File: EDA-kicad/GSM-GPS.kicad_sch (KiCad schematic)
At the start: 2 parts, among them J3 SIM-G85D1160022HHR, U9 GSM-GPS-EC25VFA-512-STD

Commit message: add caution message
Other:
- note added: "Take care when choosing variants for different continents"
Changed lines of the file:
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@@
+		)
+	)
+	(text "Take care when choosing variants for different continents"
+		(exclude_from_sim no)
+		(at 163.576 26.67 0)
+		(effects
+			(font
+				(size 1.27 1.27)
+			)
 		)
 	)

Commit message: add EG25 new gpsgsm
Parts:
- added U1: EG25GGC-128-SGNS, SPIRIT-footprints:XCVR_EG25GGC-128-SGNS, symbol SPIRIT-components:EG25GGC-128-SGNS
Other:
- moved on the sheet: U9

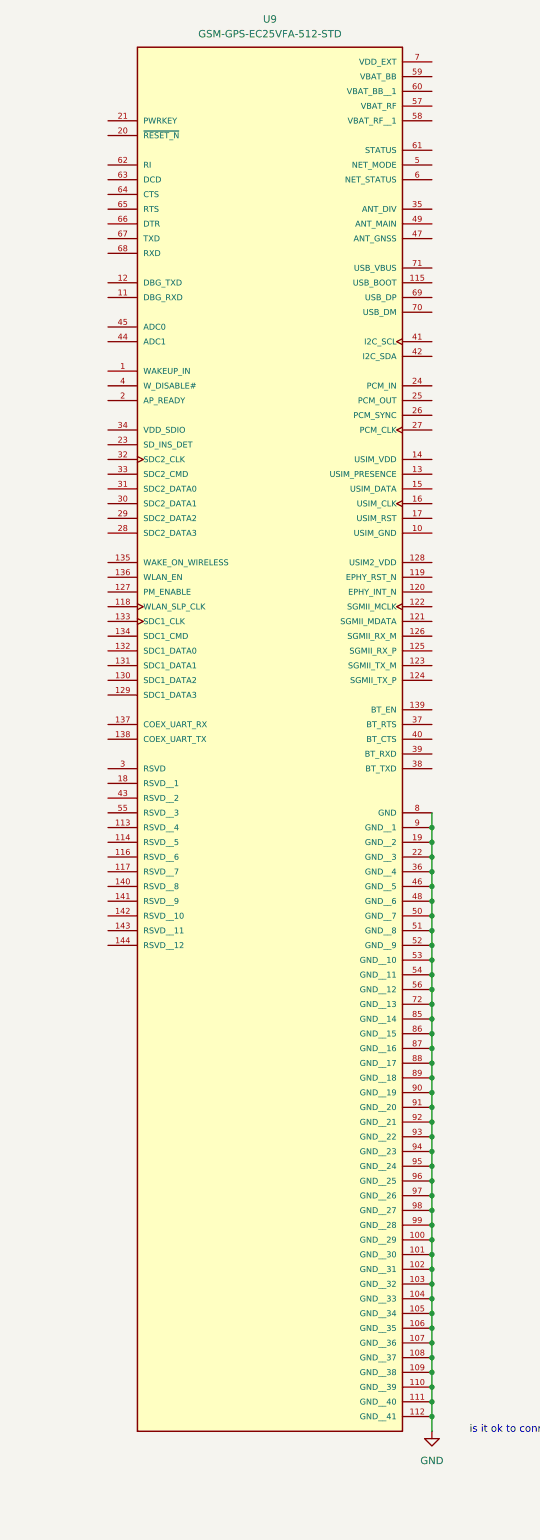
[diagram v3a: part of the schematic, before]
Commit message: exclude old EC25 and minor changes to power
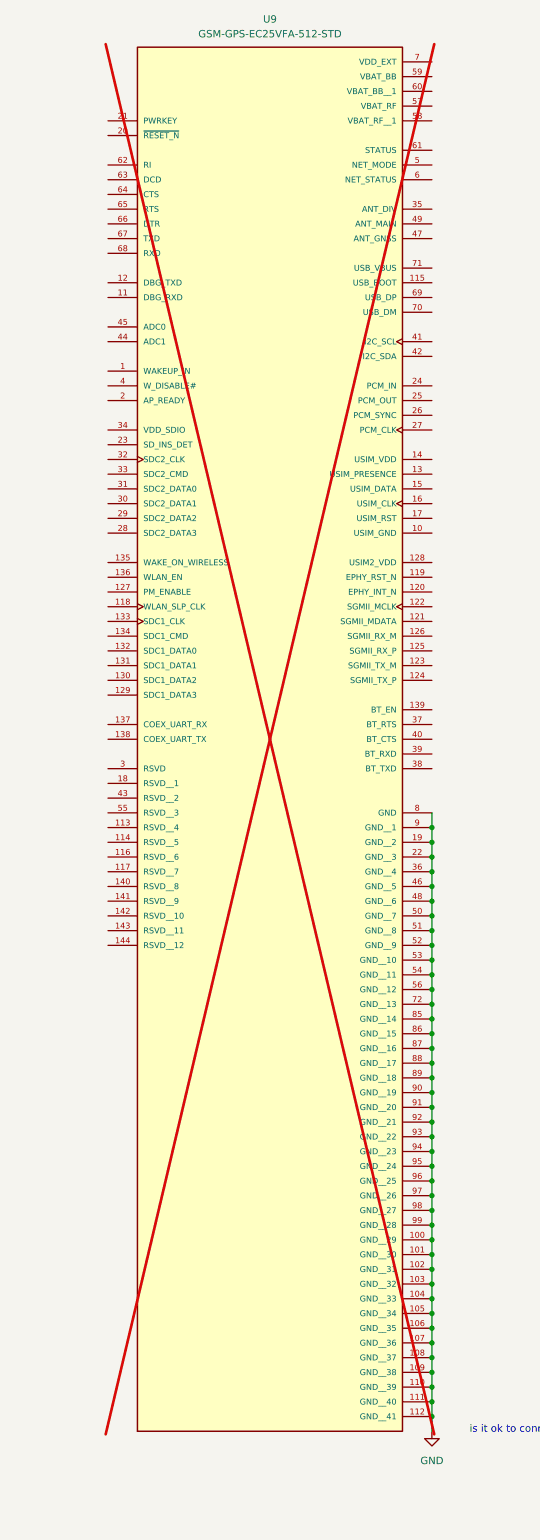
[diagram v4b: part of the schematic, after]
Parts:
- U9: now not fitted; now left out of the parts list
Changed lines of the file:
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@@
 		(unit 1)
 		(exclude_from_sim no)
-		(in_bom yes)
-		(on_board yes)
-		(dnp no)
+		(in_bom no)
+		(on_board no)
+		(dnp yes)
 		(fields_autoplaced yes)
 		(property "Reference" "U9"

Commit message: add note (test commit)
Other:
- note added: "need to be careful if 128 and 256 symbols and footprints are identical TODO rename them and double check"
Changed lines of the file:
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@@
+		)
+	)
+	(text "need to be careful if 128 and 256 symbols and footprints are identical\n\nTODO rename them and double check"
+		(exclude_from_sim no)
+		(at 168.402 84.582 0)
+		(effects
+			(font
+				(size 1.27 1.27)
+			)
 		)
 	)

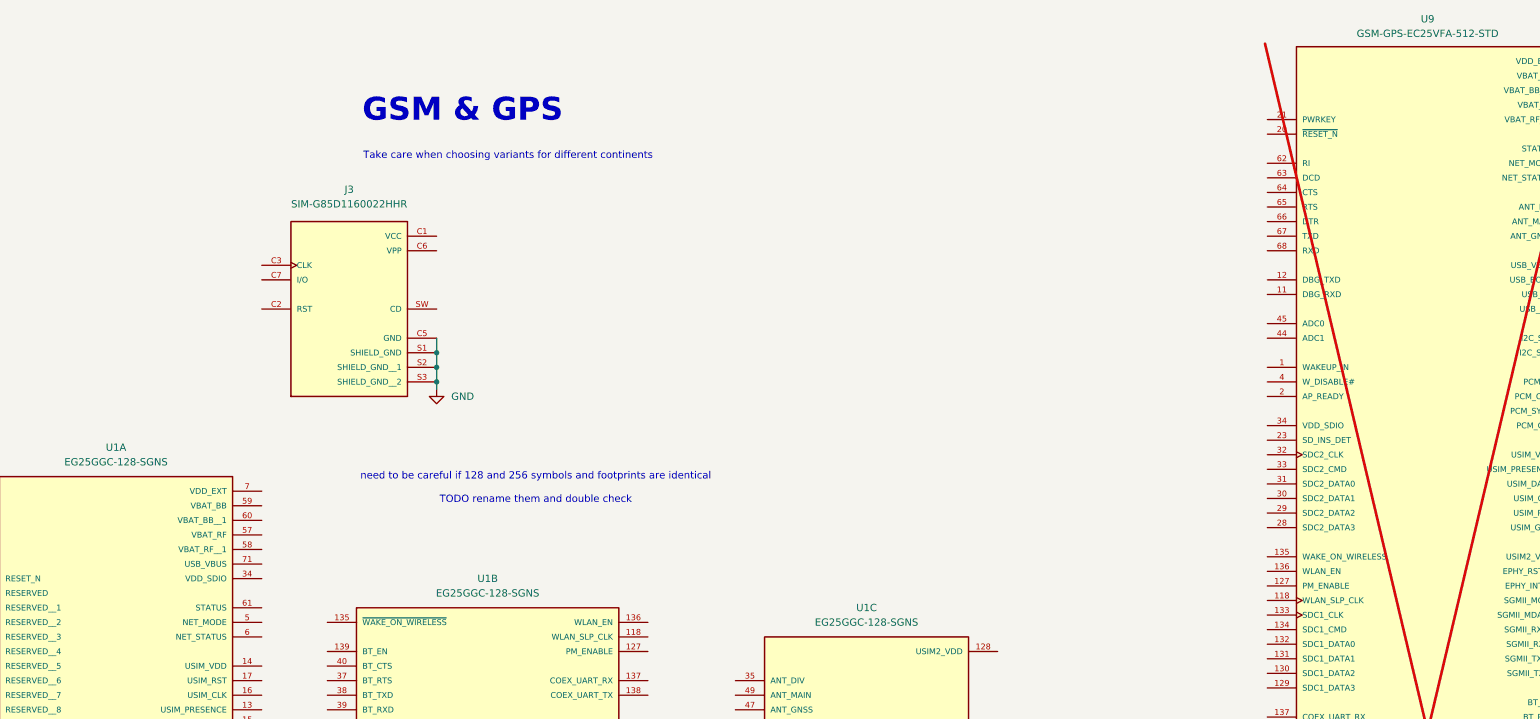
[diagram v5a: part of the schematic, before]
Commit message: reannotate entire schematic
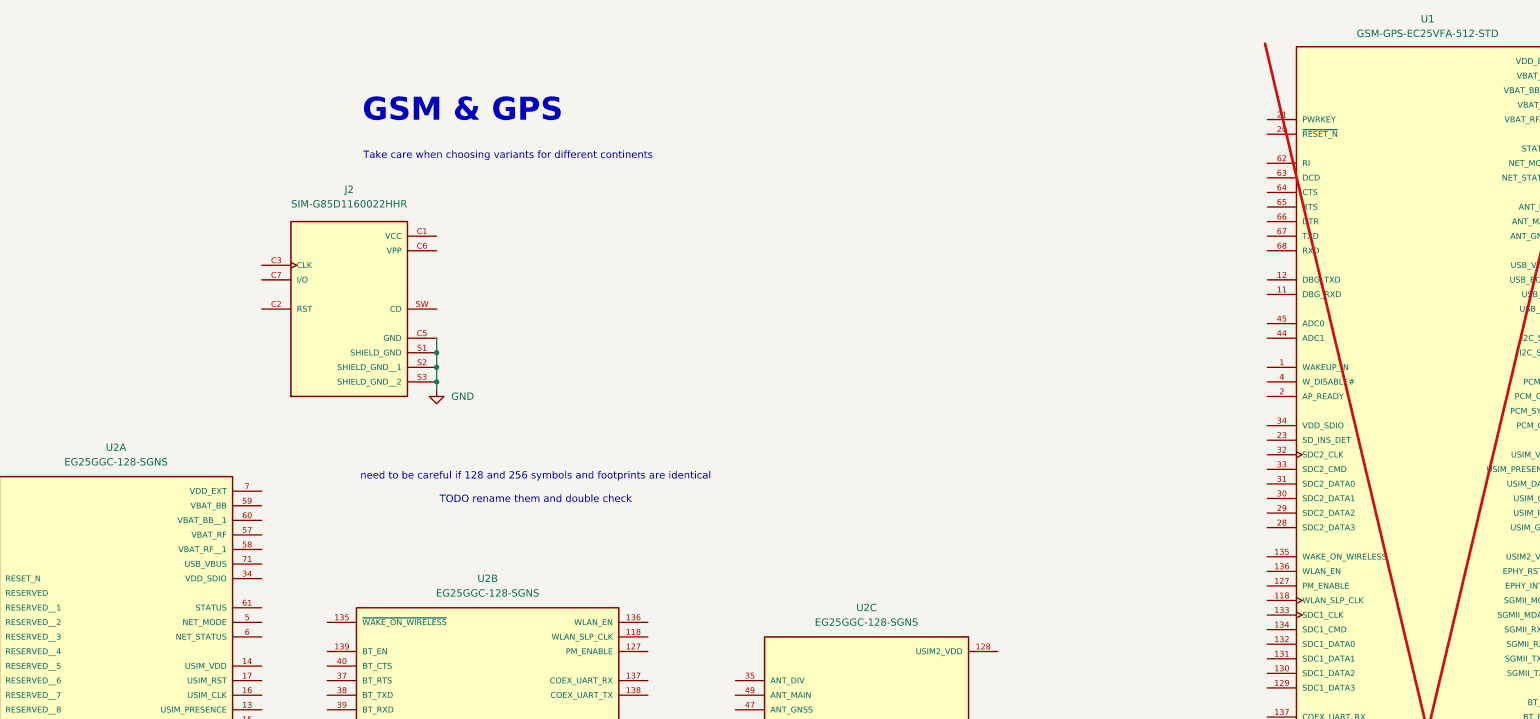
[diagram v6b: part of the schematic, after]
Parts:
- renumbered J3 to J2, U9 to U1, U1 to U2
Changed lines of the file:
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@@
 		(dnp no)
 		(fields_autoplaced yes)
-		(property "Reference" "J3"
+		(property "Reference" "J2"
 			(at 135.89 32.512 0)
 			(effects
@@
 			(project "cm5-carrier"
 				(path "/28c5e4fe-1ec7-4477-97f0-d2ec1401fad5/1297454b-0b1d-459e-9de1-2b16d7982efe"
-					(reference "J3")
+					(reference "J2")
 					(unit 1)
 				)
@@
 		(dnp no)
 		(fields_autoplaced yes)
-		(property "Reference" "U1"
+		(property "Reference" "U2"
 			(at 226.06 105.41 0)
 			(effects
@@
 			(project ""
 				(path "/28c5e4fe-1ec7-4477-97f0-d2ec1401fad5/1297454b-0b1d-459e-9de1-2b16d7982efe"
-					(reference "U1")
+					(reference "U2")
 					(unit 3)
 				)
@@
 		(dnp no)
 		(fields_autoplaced yes)
-		(property "Reference" "#PWR062"
+		(property "Reference" "#PWR063"
 			(at 151.13 73.66 0)
 			(effects
@@
 			(project "cm5-carrier"
 				(path "/28c5e4fe-1ec7-4477-97f0-d2ec1401fad5/1297454b-0b1d-459e-9de1-2b16d7982efe"
-					(reference "#PWR062")
+					(reference "#PWR063")
 					(unit 1)
 				)
@@
 		(dnp no)
 		(fields_autoplaced yes)
-		(property "Reference" "U1"
+		(property "Reference" "U2"
 			(at 95.25 77.47 0)
 			(effects
@@
 			(project ""
 				(path "/28c5e4fe-1ec7-4477-97f0-d2ec1401fad5/1297454b-0b1d-459e-9de1-2b16d7982efe"
-					(reference "U1")
+					(reference "U2")
 					(unit 1)
 				)
@@
 		(dnp yes)
 		(fields_autoplaced yes)
-		(property "Reference" "U9"
+		(property "Reference" "U1"
 			(at 323.85 2.794 0)
 			(effects
@@
 			(project "cm5-carrier"
 				(path "/28c5e4fe-1ec7-4477-97f0-d2ec1401fad5/1297454b-0b1d-459e-9de1-2b16d7982efe"
-					(reference "U9")
+					(reference "U1")
 					(unit 1)
 				)
@@
 		(dnp no)
 		(fields_autoplaced yes)
-		(property "Reference" "U1"
+		(property "Reference" "U2"
 			(at 160.02 100.33 0)
 			(effects
@@
 			(project ""
 				(path "/28c5e4fe-1ec7-4477-97f0-d2ec1401fad5/1297454b-0b1d-459e-9de1-2b16d7982efe"
-					(reference "U1")
+					(reference "U2")
 					(unit 2)
 				)
@@
 		(dnp no)
 		(fields_autoplaced yes)
-		(property "Reference" "#PWR066"
+		(property "Reference" "#PWR064"
 			(at 351.79 252.73 0)
 			(effects
@@
 			(project "cm5-carrier"
 				(path "/28c5e4fe-1ec7-4477-97f0-d2ec1401fad5/1297454b-0b1d-459e-9de1-2b16d7982efe"
-					(reference "#PWR066")
+					(reference "#PWR064")
 					(unit 1)
 				)

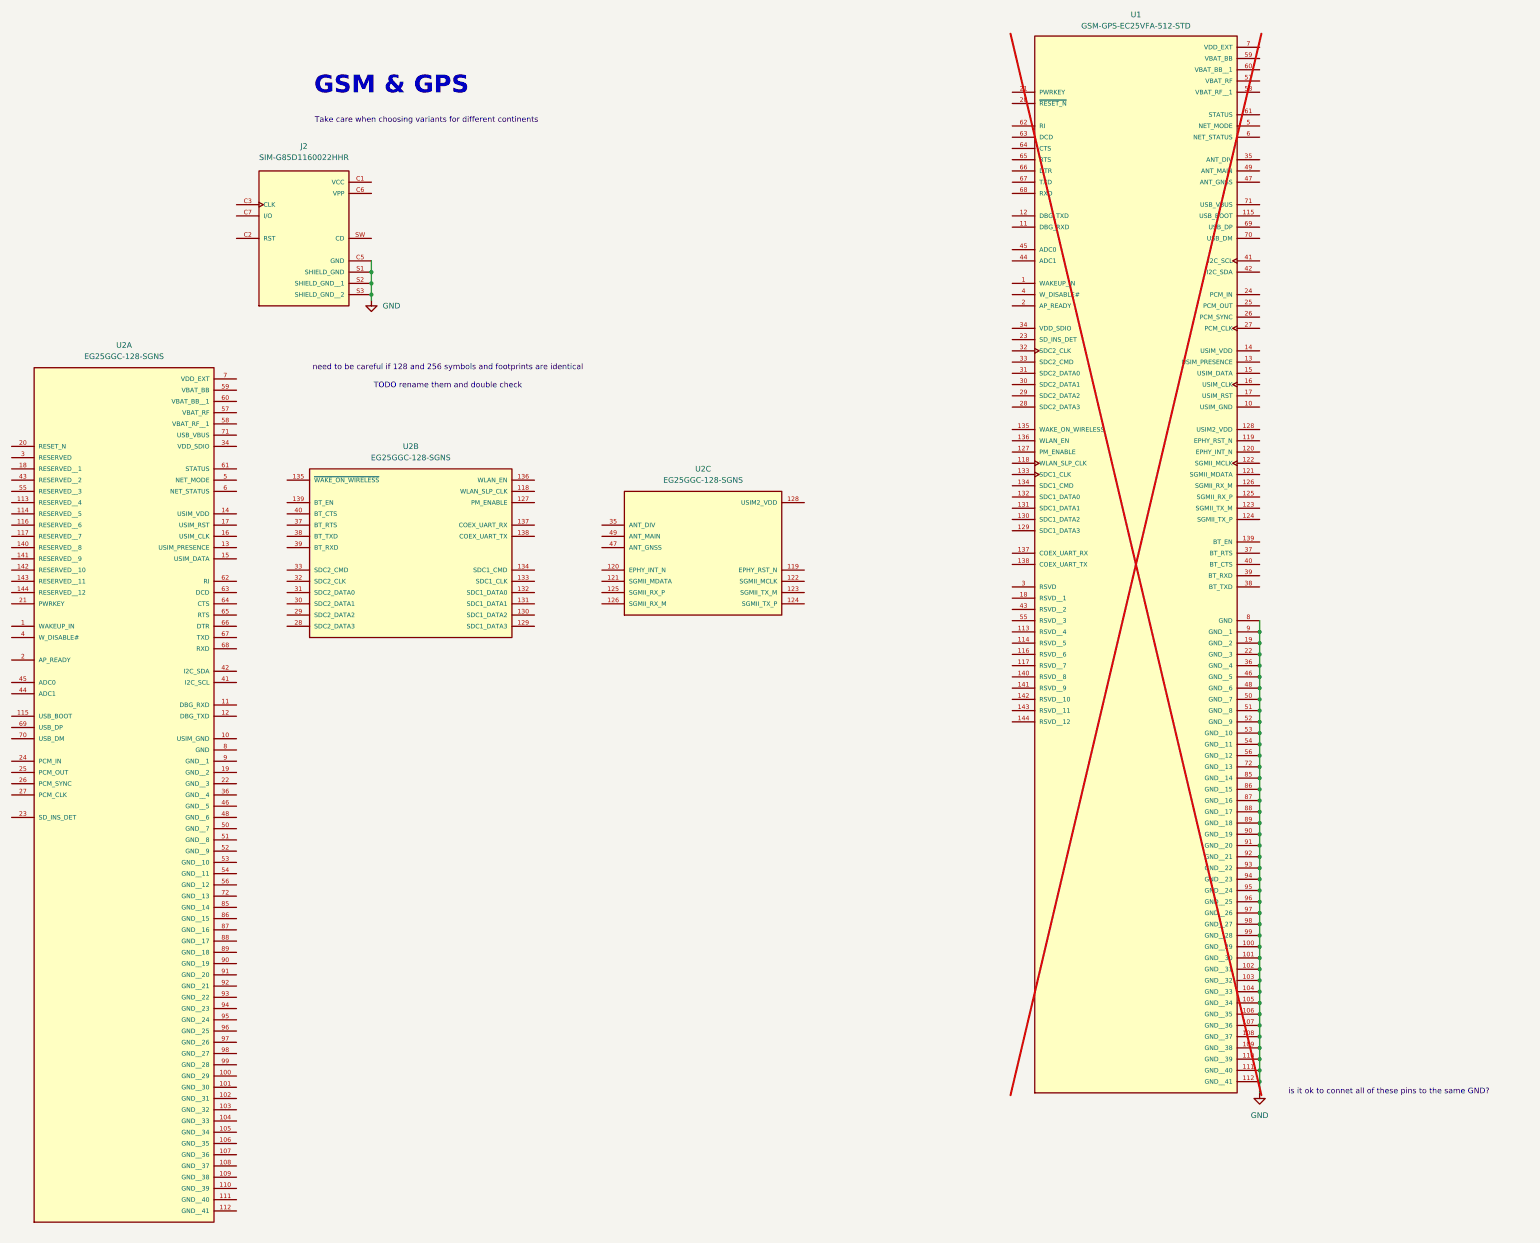
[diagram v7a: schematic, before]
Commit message: set everything except from power to DNP
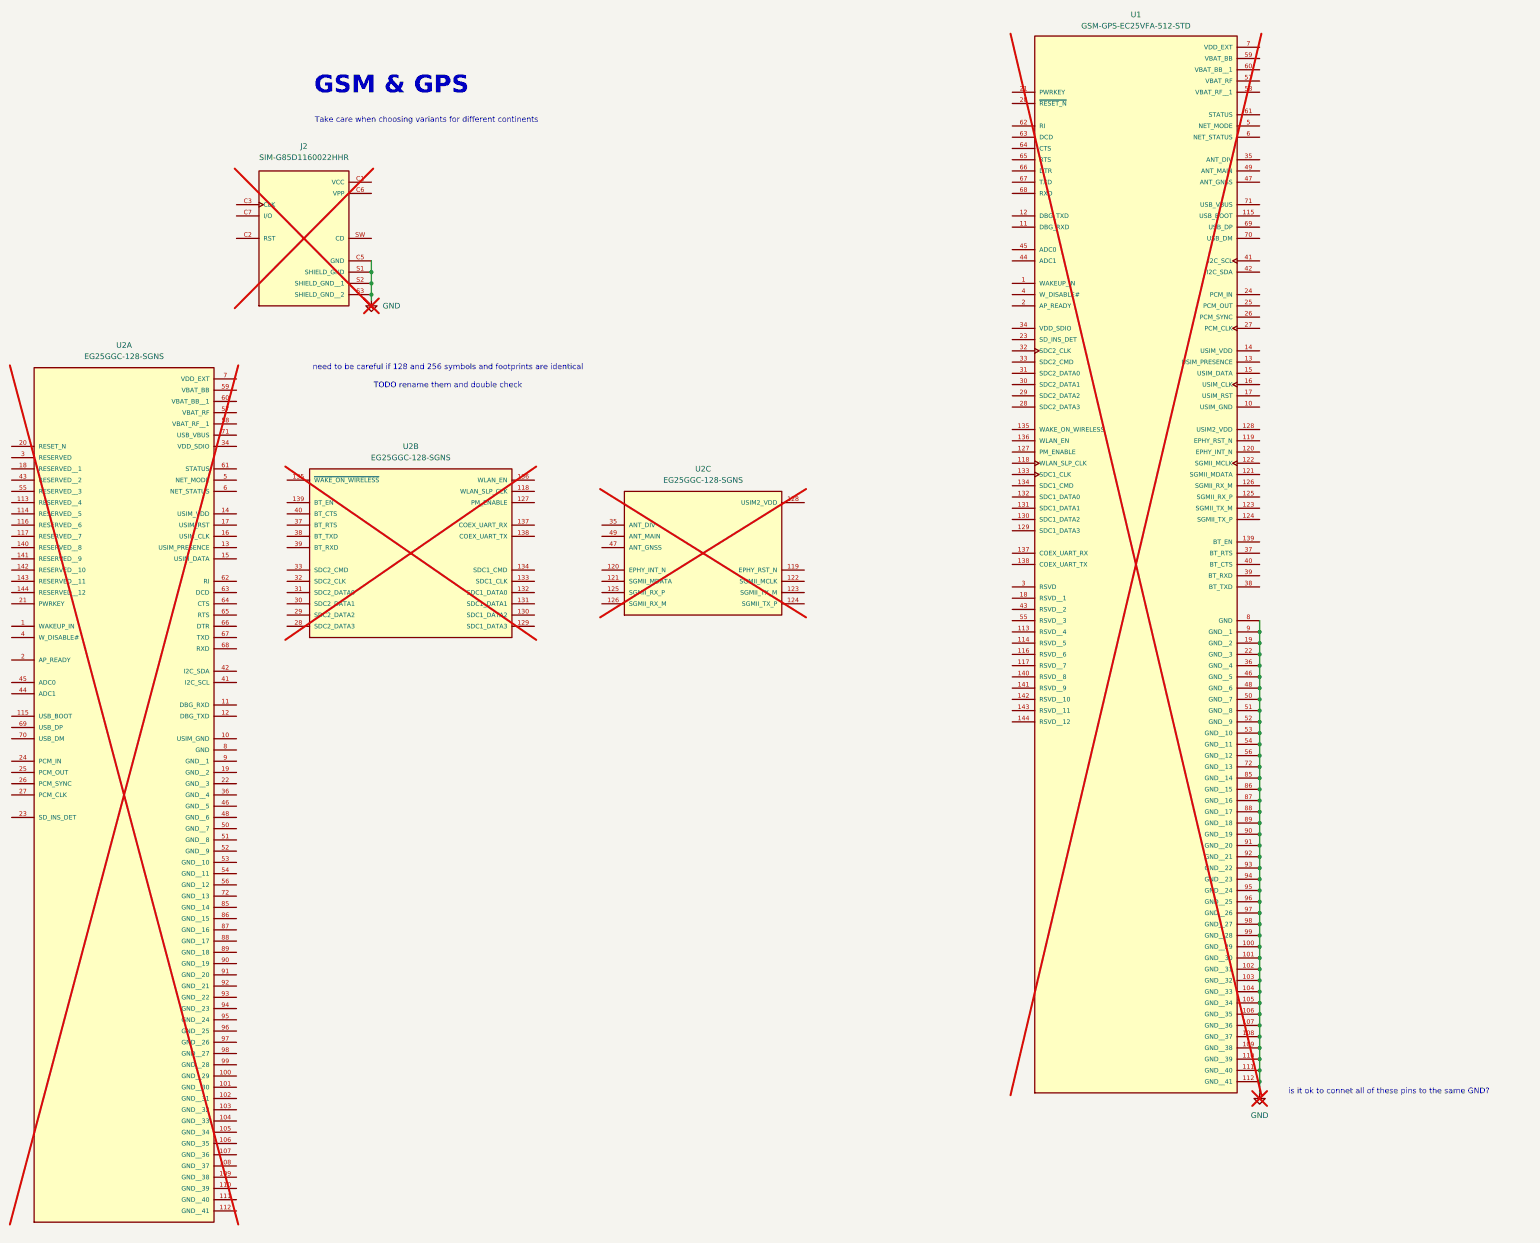
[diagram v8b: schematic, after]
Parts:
- J2, U2: now not fitted
